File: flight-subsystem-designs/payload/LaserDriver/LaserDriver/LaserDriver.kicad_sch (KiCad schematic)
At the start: 40 parts, among them J1 Input, J2 Laser 0, J3 Laser 1, J5 VIN, U1 74LVC1G04, U2 SY100ELT22ZG-TR, U3 MAX3967AETG+, U4 MAX3967AETG+, U5 NCV8161AMX330TBG

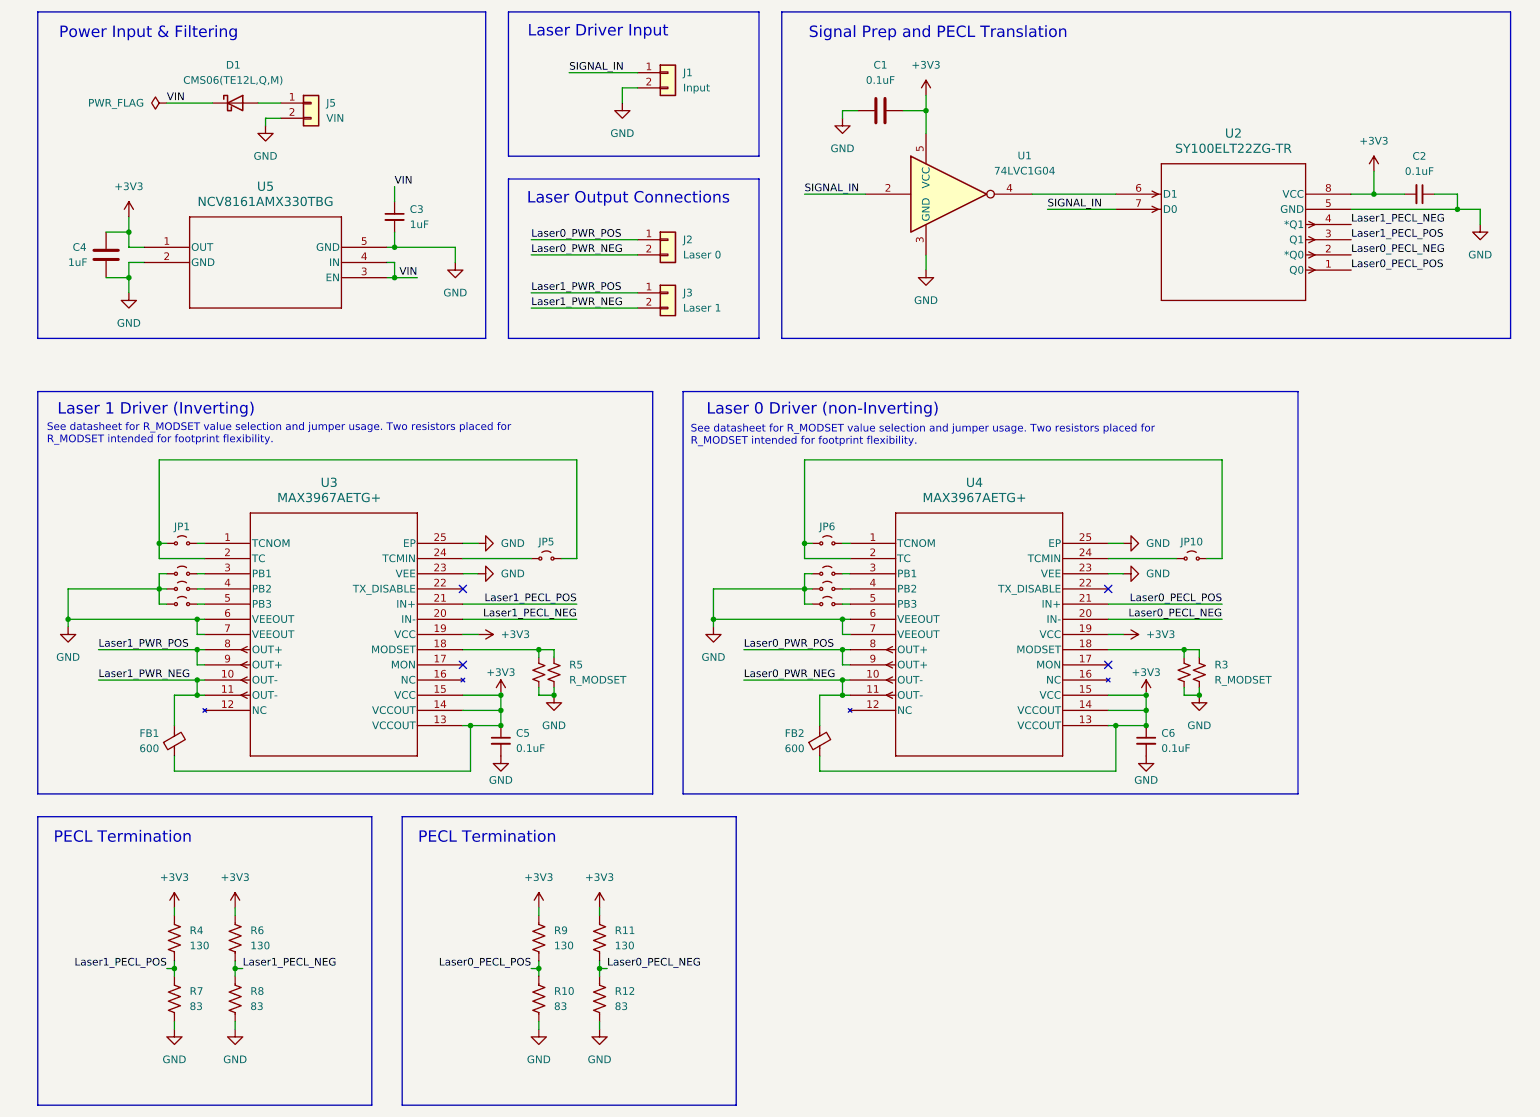
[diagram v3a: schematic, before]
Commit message: laserdriver: first board revision; changed LDO
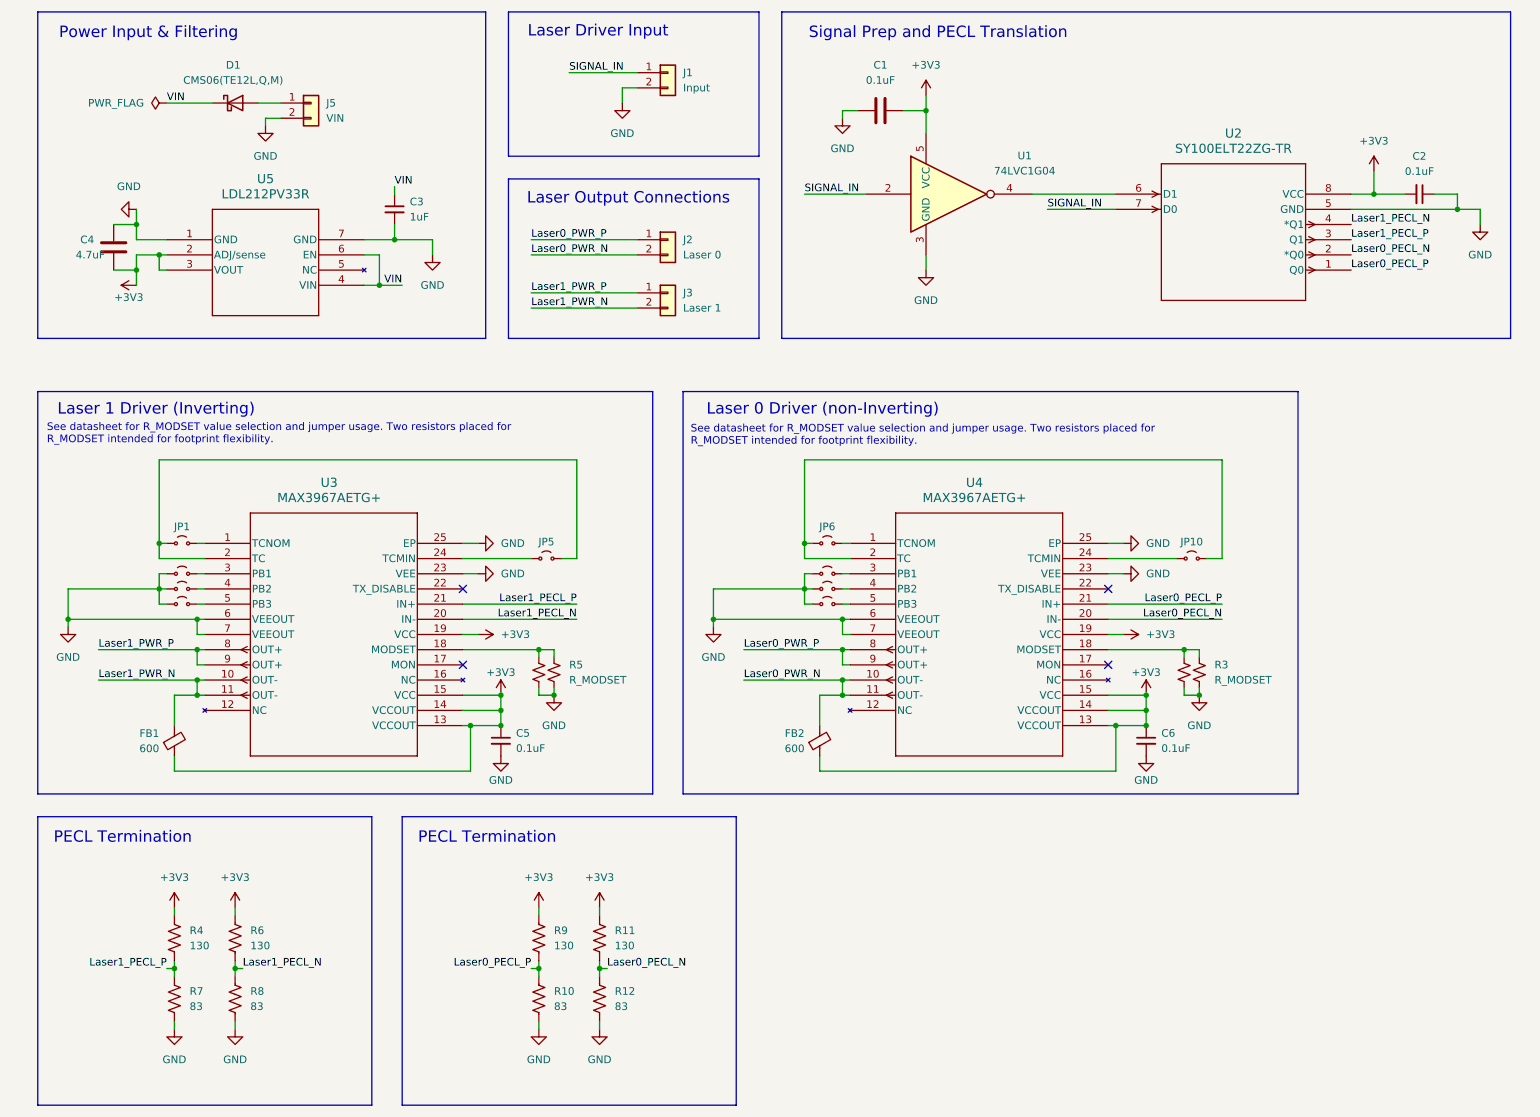
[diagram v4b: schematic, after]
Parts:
- removed U5: NCV8161AMX330TBG, footprints:XDFN4_711AJ_OSI, symbol NCV8161AMX330TBG:NCV8161AMX330TBG
- added U5: LDL212PV33R, footprints:DFN_V33R_STM, symbol LDL212PV33R:LDL212PV33R
- C4: value 1uF -> 4.7uF
- U1: footprint Resistor_SMD:R_0805_2012Metric_Pad1.20x1.40mm_HandSolder -> Package_TO_SOT_SMD:SOT-23-5_HandSoldering; DigiKeyPN (none) -> 296-11599-1-ND
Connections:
- net +3V3: now also C4.2, U5.2 (ADJ/sense), U5.3 (VOUT); no longer C4.1
- net GND: now also C4.1, U5.1 (GND), U5.7 (GND); no longer C4.2
- net VIN: now also U5.4 (VIN), U5.6 (EN)
- net Laser0_PECL_NEG renamed Laser0_PECL_N
- net Laser0_PECL_POS renamed Laser0_PECL_P
- net Laser0_PWR_NEG renamed Laser0_PWR_N
- net Laser0_PWR_POS renamed Laser0_PWR_P
- net Laser1_PECL_NEG renamed Laser1_PECL_N
- net Laser1_PECL_POS renamed Laser1_PECL_P
- net Laser1_PWR_NEG renamed Laser1_PWR_N
- net Laser1_PWR_POS renamed Laser1_PWR_P
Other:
- moved on the sheet: C3, C4

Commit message: laserdriver: add bnc and mounting holes
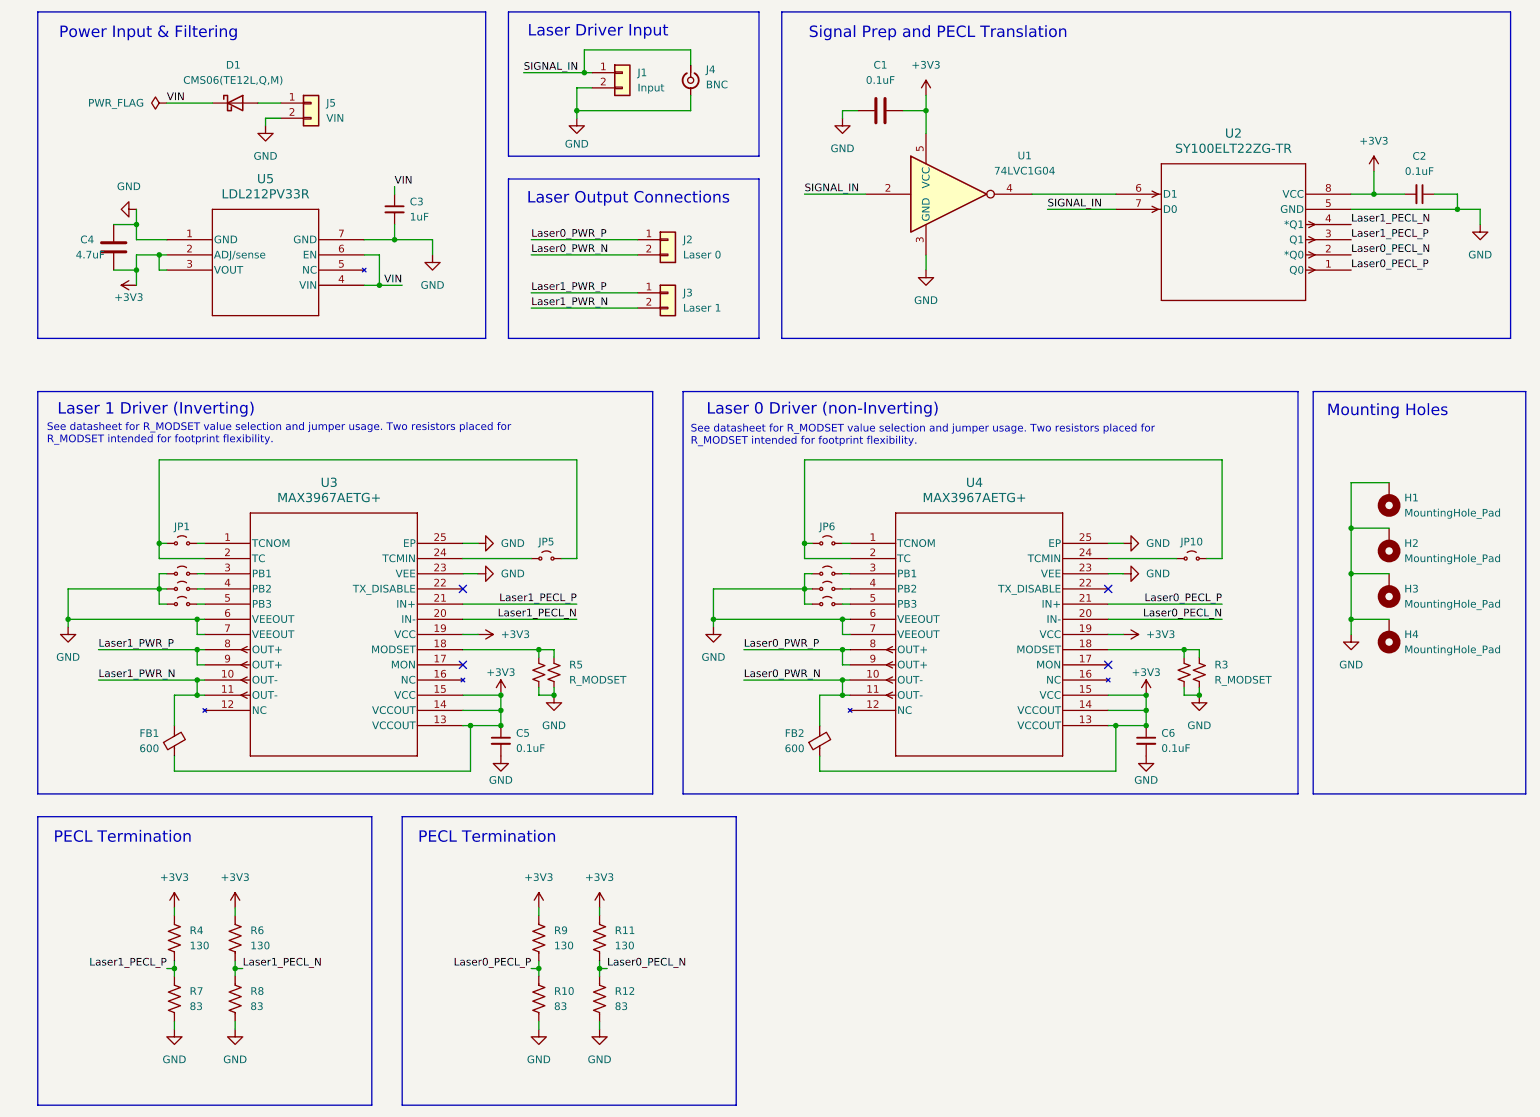
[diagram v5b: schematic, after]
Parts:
- added H1, H2, H3, H4: MountingHole_Pad, MountingHole:MountingHole_6.5mm_Pad, symbol Mechanical:MountingHole_Pad
- added J4: BNC, Connector_Coaxial:BNC_TEConnectivity_1478204_Vertical, symbol Connector:Conn_Coaxial_Small
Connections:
- net GND: now also H1.1, H2.1, H3.1, H4.1, J4.2 (Ext)
- net SIGNAL_IN: now also J4.1 (In)
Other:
- note added: "Mounting Holes"
- moved on the sheet: J1

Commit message: feat: PDU updates and laser driver v1.0.1
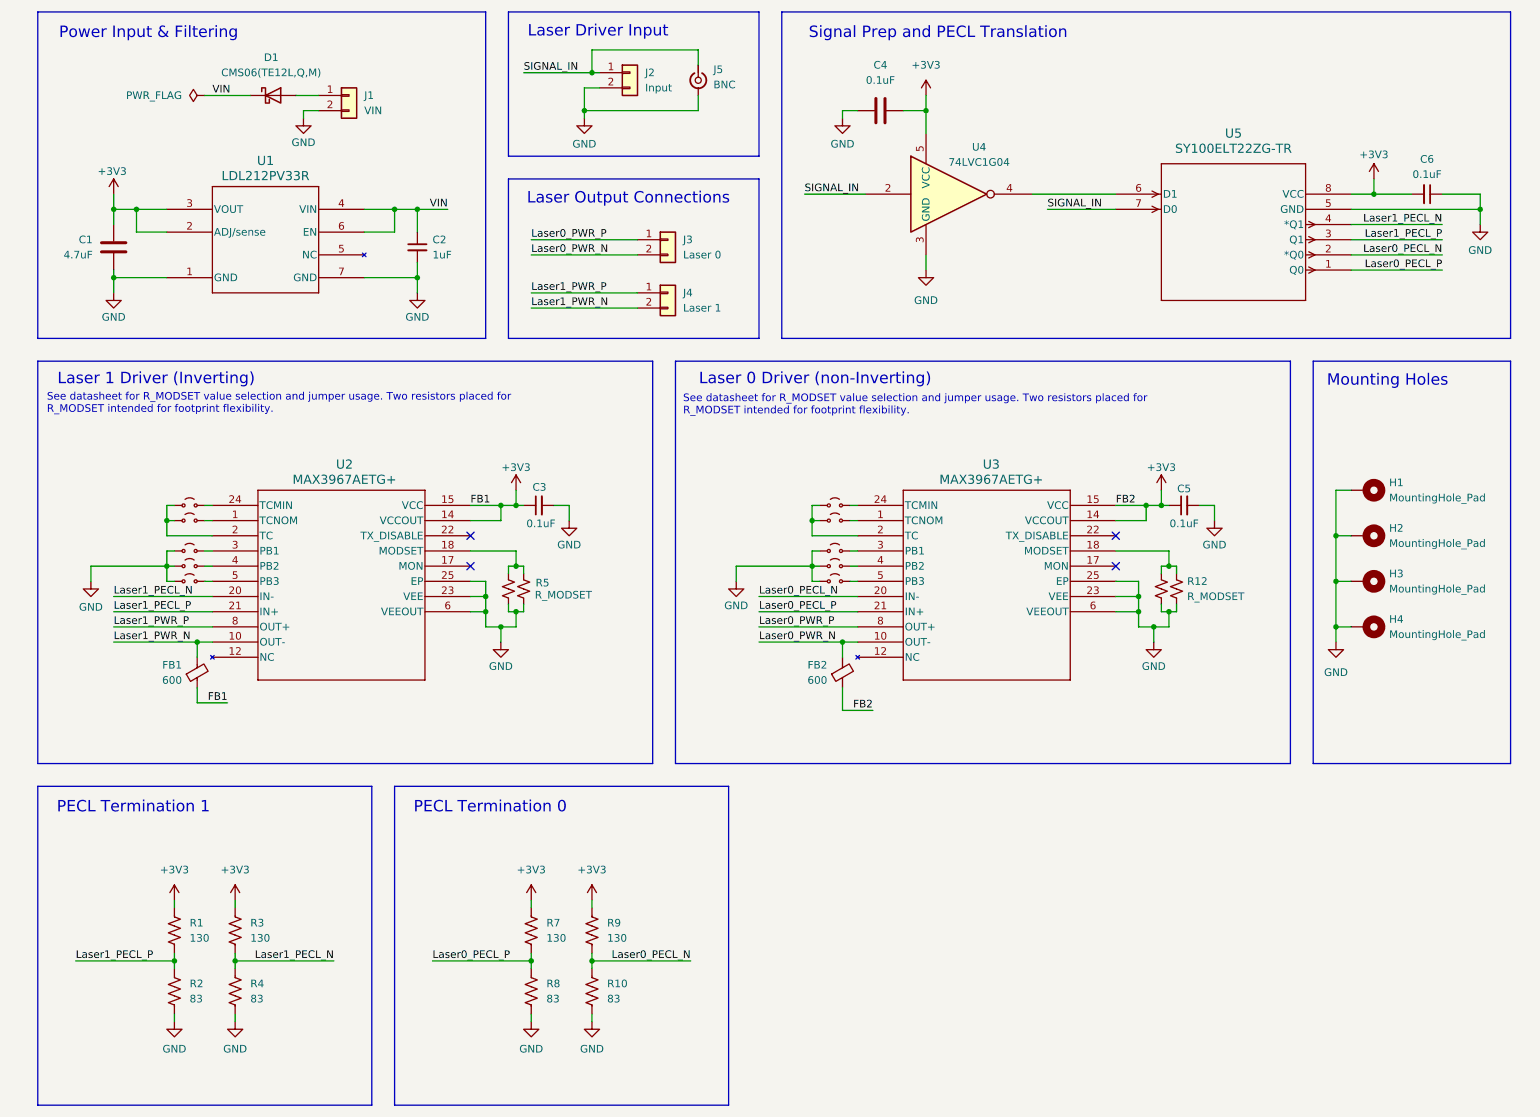
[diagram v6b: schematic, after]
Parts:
- U2: renamed from U3; footprint footprints:21-0139_T2444&plus_4_MXM -> 21-0139_T2444+4_MXM
- U3: renamed from U4; footprint footprints:21-0139_T2444&plus_4_MXM -> 21-0139_T2444+4_MXM
- renumbered C4 to C1, C3 to C2, C5 to C3, C1 to C4, C6 to C5, C2 to C6, J5 to J1, J1 to J2, J2 to J3, J3 to J4, J4 to J5, JP5 to JP1, JP9 to JP10, JP1 to JP2, JP2 to JP3, JP3 to JP4, JP4 to JP5, JP10 to JP6, JP6 to JP7, JP7 to JP8, JP8 to JP9, R4 to R1, R12 to R10, R2 to R11, R3 to R12, R7 to R2, R6 to R3, R8 to R4, R1 to R6, R9 to R7, R10 to R8, R11 to R9, U5 to U1, U1 to U4, U2 to U5
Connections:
- net +3V3: now also C1.1; no longer C1.2
- net GND: now also C1.2, R5.2, R6.2; no longer C1.1, R5.1, R6.1
- net at JP2.1 (A), U2.2 (TC): now also JP1.1 (A); no longer JP1.2 (B)
- net at U3.12 (NC): now also U3.16 (NC)
- net at JP7.1 (A), U3.2 (TC): now also JP6.1 (A); no longer JP6.2 (B)
- net at U3.24 (TCMIN): now also JP6.2 (B); no longer JP6.1 (A)
- net at U2.12 (NC): now also U2.16 (NC)
- net at U2.24 (TCMIN): now also JP1.2 (B); no longer JP1.1 (A)
- new net: R5.1, R6.1, U2.18 (MODSET)
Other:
- note added: "PECL Termination 0"
- note added: "PECL Termination 1"
- note removed: "PECL Termination"
- moved on the sheet: C2, C3, C5, C6, D1, FB1, FB2, H1, H2, H3, H4, J1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

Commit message: laserdriver: add power & input isolation
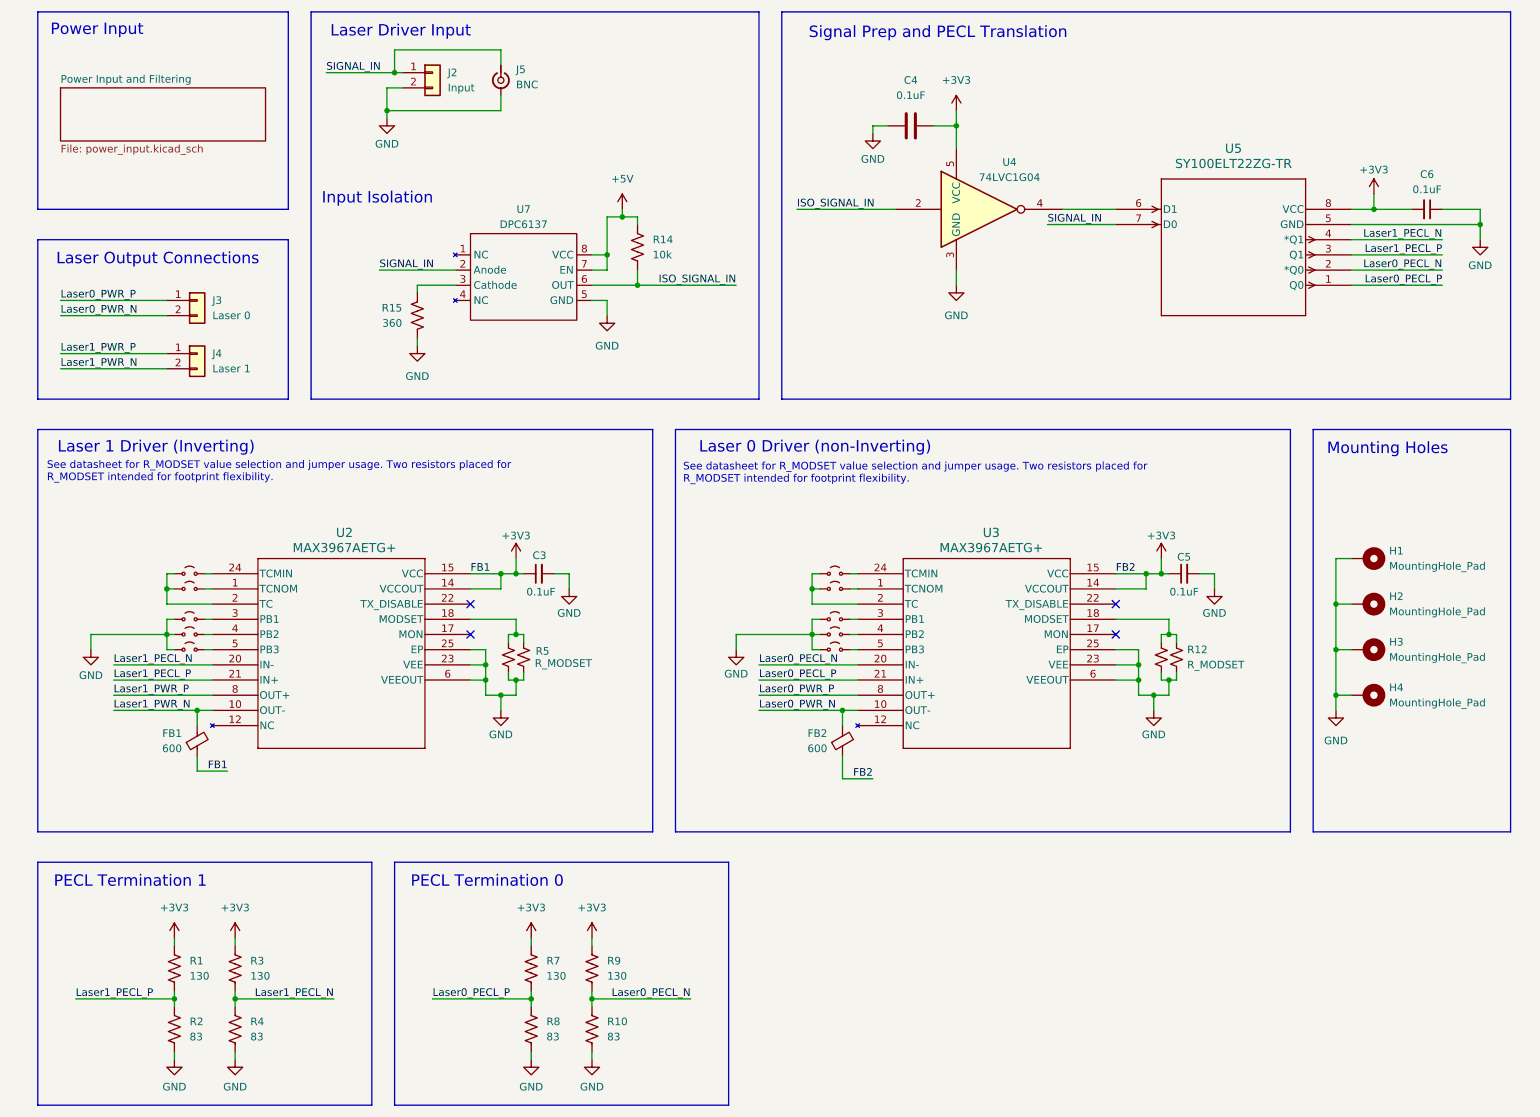
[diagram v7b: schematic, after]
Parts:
- removed C1: 4.7uF, Capacitor_SMD:C_0805_2012Metric_Pad1.18x1.45mm_HandSolder, symbol Device:C
- removed C2: 1uF, Capacitor_SMD:C_0805_2012Metric_Pad1.18x1.45mm_HandSolder, symbol Device:C_Small
- removed D1: CMS06(TE12L,Q,M), Diode_SMD:D_SOD-128, symbol Device:D_Schottky
- removed J1: VIN, Connector_PinHeader_2.54mm:PinHeader_1x02_P2.54mm_Vertical, symbol Connector_Generic:Conn_01x02
- removed U1: LDL212PV33R, footprints:DFN_V33R_STM, symbol LDL212PV33R:LDL212PV33R
- added R14: 10k, Resistor_SMD:R_0805_2012Metric, symbol Device:R_US
- added R15: 360, Resistor_SMD:R_0805_2012Metric, symbol Device:R_US
- added U7: DPC6137, Package_DIP:DIP-8_W10.16mm_LongPads, symbol CustomSymbols:DPC6137
- U2, U3: footprint 21-0139_T2444+4_MXM -> footprints:21-0139_T2444&plus_4_MXM
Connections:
- net GND: now also R15.1, U7.5 (GND)
- net SIGNAL_IN: now also U7.2 (Anode); no longer U4.2
- net at U3.12 (NC): no longer U3.16 (NC)
- net at U2.12 (NC): no longer U2.16 (NC)
- new net: R15.2, U7.3 (Cathode)
- new net +5V: R14.2, U7.7 (EN), U7.8 (VCC)
- new net ISO_SIGNAL_IN: R14.1, U4.2, U7.6 (OUT)
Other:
- added sheet Power Input and Filtering (power_input.kicad_sch)
- note added: "Input Isolation"
- note added: "Power Input"
- note removed: "Power Input & Filtering"
- moved on the sheet: C3, C4, C5, C6, FB1, FB2, H1, H2, H3, H4, J2, J3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
